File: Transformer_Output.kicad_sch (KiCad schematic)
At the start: 8 parts, among them T1 T1

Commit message: j final 2
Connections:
- net Out: now reaches +.2 (A), T1.4 (SB)
- net Out: now also +.1, CSNUB.1, T1.3 (SA), T1.6 (SD)
- net Iout: now reaches +.1, +.1 (K), C1+.1
- net Iout: now also +.2, C1+.2, T1.1 (AA)
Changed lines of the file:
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@@
+		)
+	)
+	(hierarchical_label "Iout"
+		(shape input)
+		(at 228.6 99.06 90)
+		(effects
+			(font
+				(size 1.27 1.27)
+			)
+			(justify left)
+		)
+	)
+	(hierarchical_label "Out"
+		(shape input)
+		(at 49.53 44.45 180)
+		(effects
+			(font
+				(size 1.27 1.27)
+			)
+			(justify right)
+		)
+	)
+	(hierarchical_label "Out"
+		(shape input)
+		(at 132.08 139.7 270)
+		(effects
+			(font
+				(size 1.27 1.27)
+			)
+			(justify right)
+		)
+	)
+	(hierarchical_label "Out"
+		(shape input)
+		(at 93.98 101.6 270)
+		(effects
+			(font
+				(size 1.27 1.27)
+			)
+			(justify right)
+		)
+	)
+	(hierarchical_label "Iout"
+		(shape input)
+		(at 228.6 86.36 270)
+		(effects
+			(font
+				(size 1.27 1.27)
+			)
+			(justify right)
 		)
 	)

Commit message: j final 3
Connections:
- net Iout renamed I_In
- net I_In: no longer +.2, C1+.2, T1.1 (AA)
- net Out renamed Rectifier_In
- net Rectifier_In: no longer +.2 (A), T1.4 (SB), T1.6 (SD)
- new net Chip_In: +.2 (A), T1.4 (SB)
- new net I_Out: +.2, C1+.2, T1.1 (AA)
- new net Transformer_Out: T1.6 (SD)
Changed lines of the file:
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@@
 		)
 	)
-	(hierarchical_label "Iout"
+	(hierarchical_label "I_Out"
 		(shape input)
 		(at 228.6 99.06 90)
@@
 		)
 	)
-	(hierarchical_label "Out"
+	(hierarchical_label "Rectifier_In"
 		(shape input)
 		(at 49.53 44.45 180)
@@
 		)
 	)
-	(hierarchical_label "Out"
+	(hierarchical_label "Transformer_Out"
 		(shape input)
 		(at 132.08 139.7 270)
@@
 		)
 	)
-	(hierarchical_label "Out"
+	(hierarchical_label "Chip_In"
 		(shape input)
 		(at 93.98 101.6 270)
@@
 		)
 	)
-	(hierarchical_label "Iout"
+	(hierarchical_label "I_In"
 		(shape input)
 		(at 228.6 86.36 270)

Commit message: Added sheet pins
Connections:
- net Chip_In renamed Mosfet_Snub
- net I_In renamed Main_Output
- net I_Out renamed Rectifier_GND
- net Transformer_Out renamed Zener_UCC_Chip
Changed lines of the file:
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@@
 	(wire
 		(pts
-			(xy 228.6 77.47) (xy 228.6 86.36)
+			(xy 237.49 77.47) (xy 237.49 87.63)
 		)
 		(stroke
@@
 	(wire
 		(pts
-			(xy 228.6 99.06) (xy 228.6 111.76)
+			(xy 242.57 109.22) (xy 242.57 111.76)
 		)
 		(stroke
@@
 	(wire
 		(pts
-			(xy 208.28 77.47) (xy 228.6 77.47)
+			(xy 208.28 77.47) (xy 237.49 77.47)
 		)
 		(stroke
@@
 	(wire
 		(pts
-			(xy 208.28 111.76) (xy 228.6 111.76)
+			(xy 208.28 111.76) (xy 242.57 111.76)
 		)
 		(stroke
@@
 		)
 	)
-	(hierarchical_label "I_Out"
+	(hierarchical_label "Rectifier_GND"
 		(shape input)
-		(at 228.6 99.06 90)
+		(at 242.57 109.22 90)
 		(effects
 			(font
@@
 		)
 	)
-	(hierarchical_label "Transformer_Out"
+	(hierarchical_label "Zener_UCC_Chip"
 		(shape input)
 		(at 132.08 139.7 270)
@@
 		)
 	)
-	(hierarchical_label "Chip_In"
+	(hierarchical_label "Mosfet_Snub"
 		(shape input)
 		(at 93.98 101.6 270)
@@
 		)
 	)
-	(hierarchical_label "I_In"
+	(hierarchical_label "Main_Output"
 		(shape input)
-		(at 228.6 86.36 270)
+		(at 237.49 87.63 270)
 		(effects
 			(font

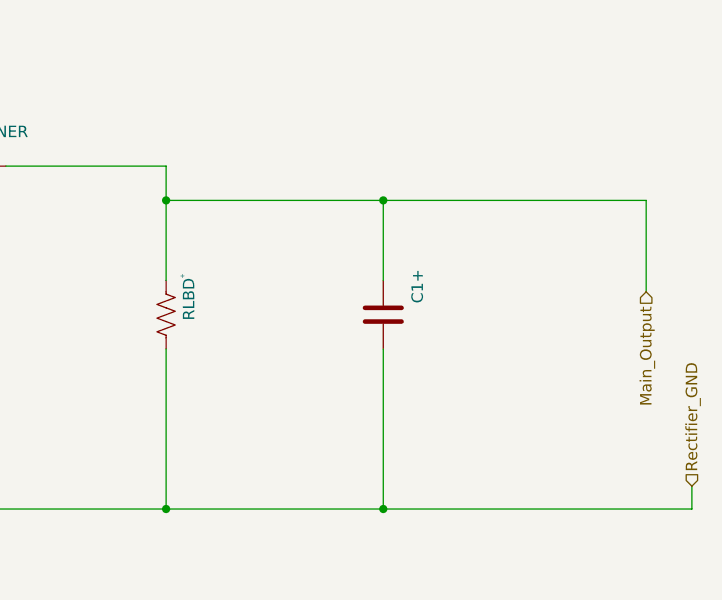
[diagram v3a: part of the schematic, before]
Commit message: Mosfet&UCC
Added Mosfet with label and rewired the UCC chip
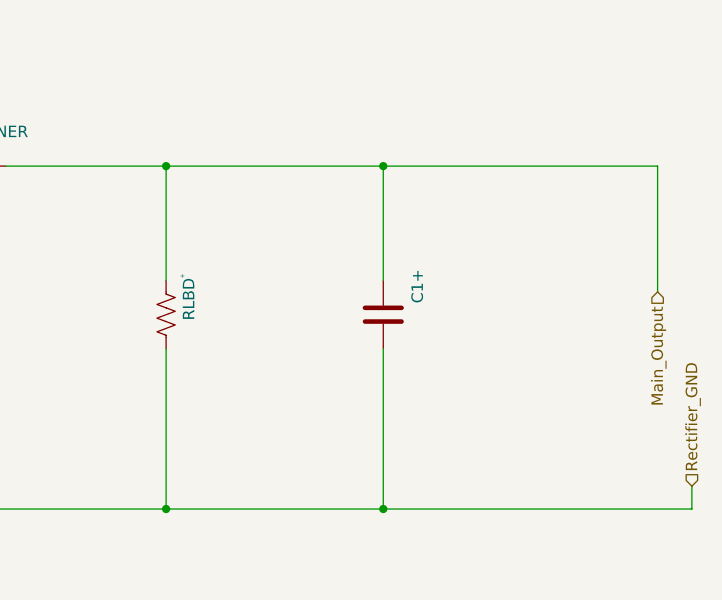
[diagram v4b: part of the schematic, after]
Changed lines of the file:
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@@
 	)
 	(junction
-		(at 208.28 77.47)
+		(at 208.28 73.66)
 		(diameter 0)
 		(color 0 0 0 0)
@@
 	)
 	(junction
-		(at 184.15 77.47)
+		(at 184.15 73.66)
 		(diameter 0)
 		(color 0 0 0 0)
@@
 	(wire
 		(pts
-			(xy 184.15 86.36) (xy 184.15 77.47)
+			(xy 184.15 73.66) (xy 184.15 86.36)
 		)
 		(stroke
@@
 	(wire
 		(pts
-			(xy 184.15 77.47) (xy 208.28 77.47)
+			(xy 184.15 73.66) (xy 208.28 73.66)
 		)
 		(stroke
@@
 	(wire
 		(pts
-			(xy 184.15 73.66) (xy 184.15 77.47)
-		)
-		(stroke
-			(width 0)
-			(type default)
-		)
-	)
-	(wire
-		(pts
 			(xy 93.98 59.69) (xy 93.98 62.23)
 		)
@@
 	(wire
 		(pts
-			(xy 237.49 77.47) (xy 237.49 87.63)
+			(xy 238.76 73.66) (xy 238.76 87.63)
 		)
 		(stroke
@@
 	(wire
 		(pts
-			(xy 208.28 77.47) (xy 237.49 77.47)
+			(xy 208.28 73.66) (xy 238.76 73.66)
 		)
 		(stroke
@@
 	(wire
 		(pts
-			(xy 208.28 77.47) (xy 208.28 86.36)
+			(xy 208.28 73.66) (xy 208.28 86.36)
 		)
 		(stroke
@@
 	(hierarchical_label "Main_Output"
 		(shape input)
-		(at 237.49 87.63 270)
+		(at 238.76 87.63 270)
 		(effects
 			(font

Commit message: change
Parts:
- C1+1: renamed from C1+; footprint Package_SON:Texas_DSG0008A_WSON-8-1EP_2x2mm_P0.5mm_EP0.9x1.6mm -> Capacitor_THT:C_Disc_D5.0mm_W2.5mm_P2.50mm
- CSNUB1: renamed from CSNUB; footprint (none) -> Capacitor_THT:C_Disc_D5.0mm_W2.5mm_P2.50mm
- T1: footprint (none) -> Transformer_THT:Transformer_Toroid_Tapped_Horizontal_D10.5mm_Amidon-T37
- renumbered + to +1, + to +2, + to +3, + to +4, + to +5
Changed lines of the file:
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@@
 		(dnp no)
 		(fields_autoplaced yes)
-		(property "Reference" "#PWR01"
+		(property "Reference" "#PWR015"
 			(at 119.38 106.68 0)
 			(hide yes)
@@
 			(project "Solar_Battery"
 				(path "/6805959e-39bb-4644-b93e-3970e29fedc0/a320594e-eb17-43a9-8193-2f75b3718179/7e488579-baf6-4b9f-affb-a6601b6eb832"
-					(reference "#PWR01")
+					(reference "#PWR015")
 					(unit 1)
 				)
@@
 		(in_pos_files yes)
 		(dnp no)
-		(property "Reference" "+"
+		(property "Reference" "+2"
 			(at 91.44 86.106 0)
 			(show_name no)
@@
 			(project "Solar_Battery"
 				(path "/6805959e-39bb-4644-b93e-3970e29fedc0/a320594e-eb17-43a9-8193-2f75b3718179/7e488579-baf6-4b9f-affb-a6601b6eb832"
-					(reference "+")
+					(reference "+2")
 					(unit 1)
 				)
@@
 		(in_pos_files yes)
 		(dnp no)
-		(property "Reference" "C1+"
+		(property "Reference" "C1+1"
 			(at 212.09 88.8999 90)
 			(show_name no)
@@
 			)
 		)
-		(property "Footprint" "Package_SON:Texas_DSG0008A_WSON-8-1EP_2x2mm_P0.5mm_EP0.9x1.6mm"
+		(property "Footprint" "Capacitor_THT:C_Disc_D5.0mm_W2.5mm_P2.50mm"
 			(at 209.2452 93.98 0)
 			(hide yes)
@@
 			(project "Solar_Battery"
 				(path "/6805959e-39bb-4644-b93e-3970e29fedc0/a320594e-eb17-43a9-8193-2f75b3718179/7e488579-baf6-4b9f-affb-a6601b6eb832"
-					(reference "C1+")
+					(reference "C1+1")
 					(unit 1)
 				)
@@
 		(in_pos_files yes)
 		(dnp no)
-		(property "Reference" "CSNUB"
+		(property "Reference" "CSNUB1"
 			(at 84.328 55.118 0)
 			(show_name no)
@@
 			)
 		)
-		(property "Footprint" ""
+		(property "Footprint" "Capacitor_THT:C_Disc_D5.0mm_W2.5mm_P2.50mm"
 			(at 94.9452 59.69 0)
 			(hide yes)
@@
 			(project "Solar_Battery"
 				(path "/6805959e-39bb-4644-b93e-3970e29fedc0/a320594e-eb17-43a9-8193-2f75b3718179/7e488579-baf6-4b9f-affb-a6601b6eb832"
-					(reference "CSNUB")
+					(reference "CSNUB1")
 					(unit 1)
 				)
@@
 		(in_pos_files yes)
 		(dnp no)
-		(property "Reference" "+"
+		(property "Reference" "+5"
 			(at 185.674 85.852 0)
 			(show_name no)
@@
 			(project "Solar_Battery"
 				(path "/6805959e-39bb-4644-b93e-3970e29fedc0/a320594e-eb17-43a9-8193-2f75b3718179/7e488579-baf6-4b9f-affb-a6601b6eb832"
-					(reference "+")
+					(reference "+5")
 					(unit 1)
 				)
@@
 		(in_pos_files yes)
 		(dnp no)
-		(property "Reference" "+"
+		(property "Reference" "+1"
 			(at 104.394 75.692 0)
 			(show_name no)
@@
 			(project "Solar_Battery"
 				(path "/6805959e-39bb-4644-b93e-3970e29fedc0/a320594e-eb17-43a9-8193-2f75b3718179/7e488579-baf6-4b9f-affb-a6601b6eb832"
-					(reference "+")
+					(reference "+1")
 					(unit 1)
 				)
@@
 		(in_pos_files yes)
 		(dnp no)
-		(property "Reference" "+"
+		(property "Reference" "+4"
 			(at 159.258 70.866 0)
 			(show_name no)
@@
 			(project "Solar_Battery"
 				(path "/6805959e-39bb-4644-b93e-3970e29fedc0/a320594e-eb17-43a9-8193-2f75b3718179/7e488579-baf6-4b9f-affb-a6601b6eb832"
-					(reference "+")
+					(reference "+4")
 					(unit 1)
 				)
@@
 			)
 		)
-		(property "Footprint" ""
+		(property "Footprint" "Transformer_THT:Transformer_Toroid_Tapped_Horizontal_D10.5mm_Amidon-T37"
 			(at 146.05 83.82 0)
 			(hide yes)
@@
 		(in_pos_files yes)
 		(dnp no)
-		(property "Reference" "+"
+		(property "Reference" "+3"
 			(at 123.444 55.372 0)
 			(show_name no)
@@
 			(project "Solar_Battery"
 				(path "/6805959e-39bb-4644-b93e-3970e29fedc0/a320594e-eb17-43a9-8193-2f75b3718179/7e488579-baf6-4b9f-affb-a6601b6eb832"
-					(reference "+")
-					(unit 1)
-				)
+					(reference "+3")
+					(unit 1)
+				)
